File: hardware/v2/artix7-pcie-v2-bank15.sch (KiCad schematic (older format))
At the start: 1 part, among them U1 XC7A75T-FGG484

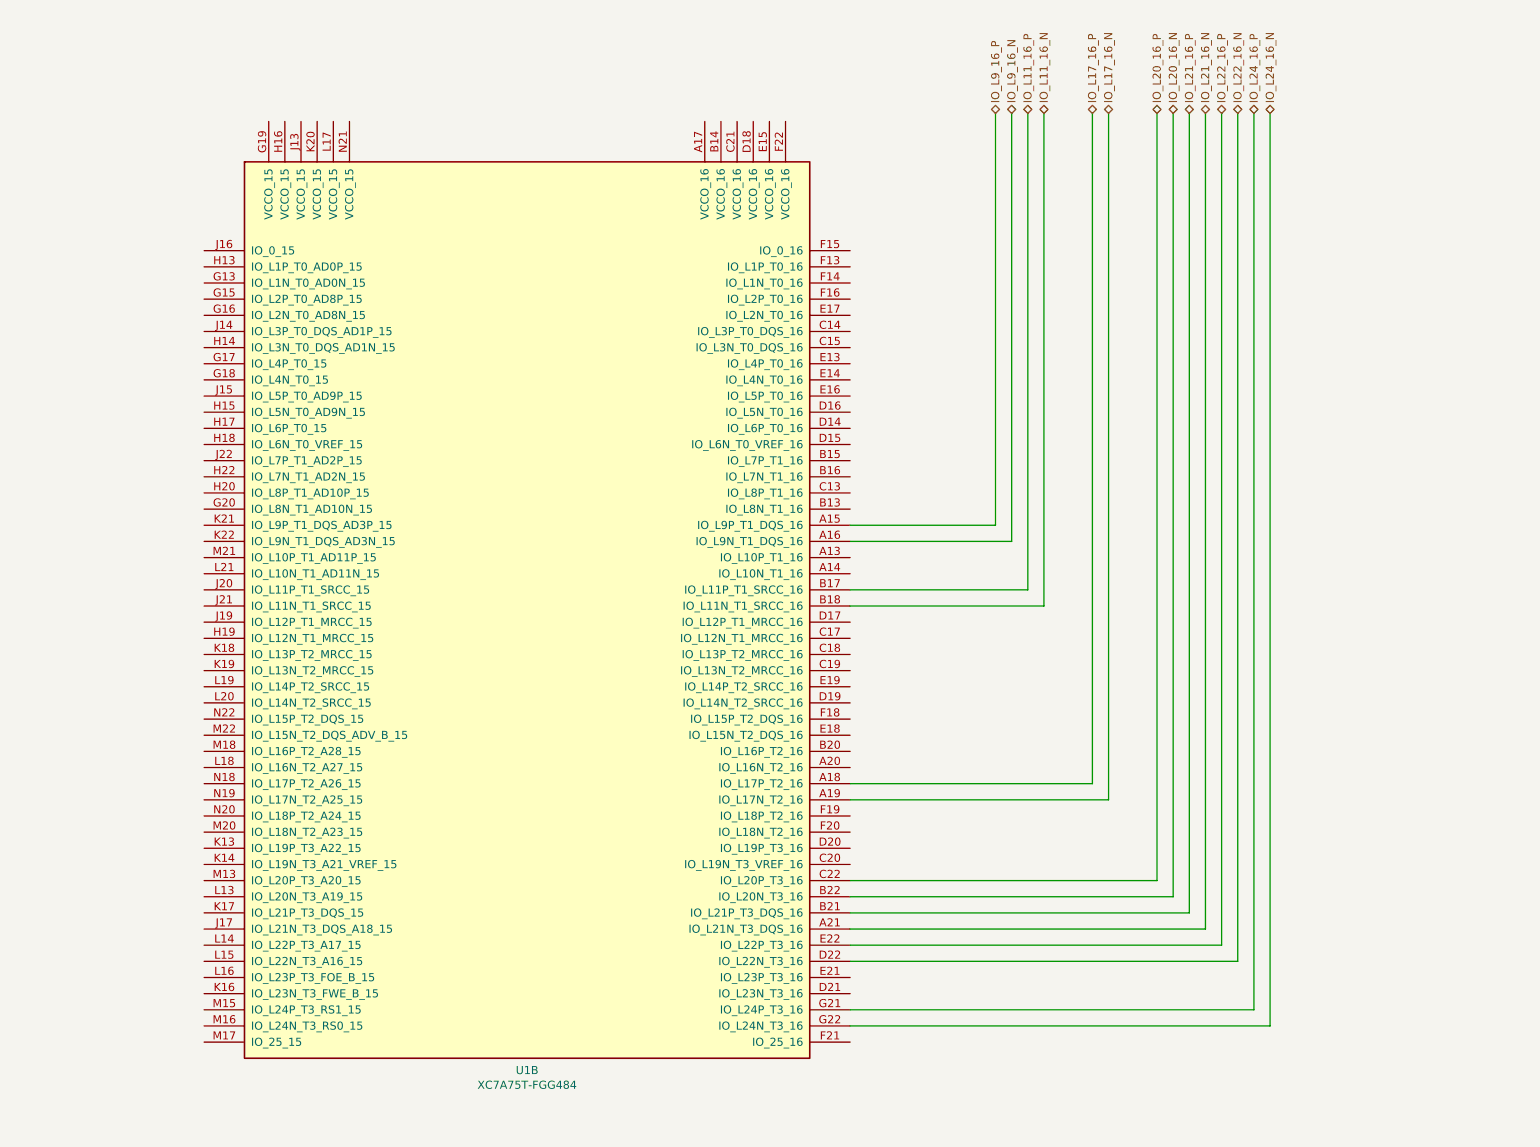
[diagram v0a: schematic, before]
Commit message: v2 schematic/pcb: band 13 to NC for smaller device compatibility
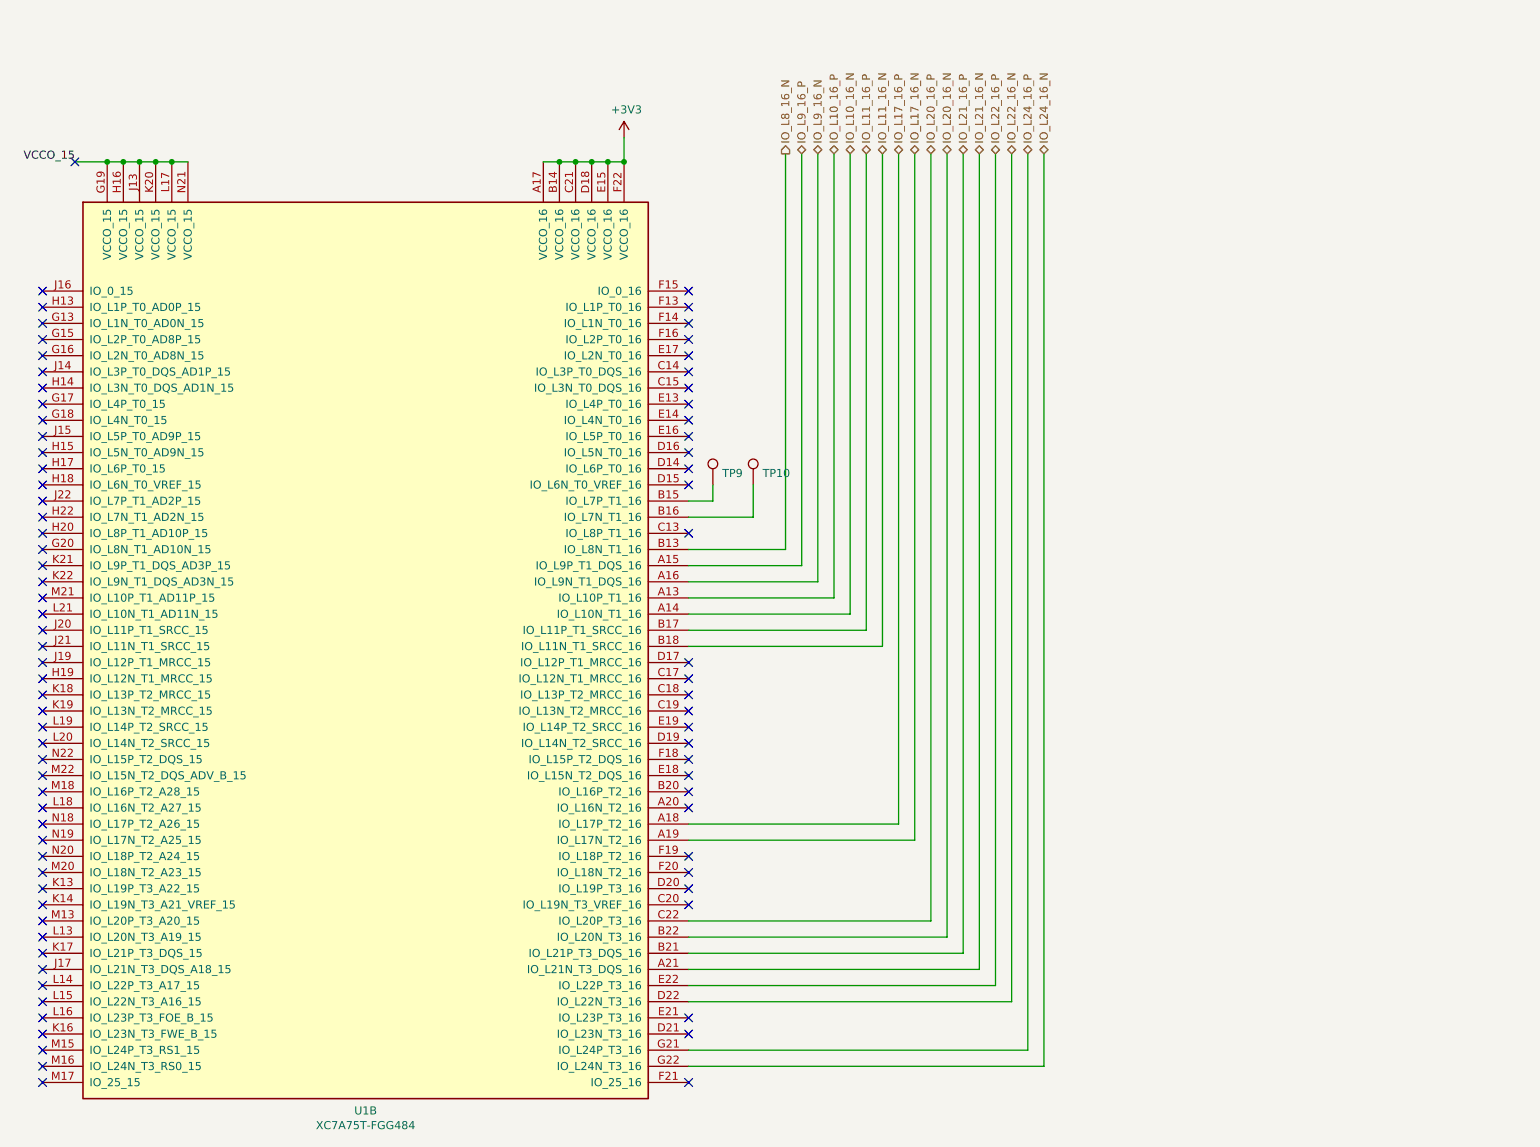
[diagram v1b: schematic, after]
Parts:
- added TP10, TP9: TestPoint, tom-mechanical:TestPoint_Pad_D1.5mm, symbol tom-mechanical:TestPoint
- U1: footprint (none) -> artix7-pcie-v2:Xilinx_FGG484
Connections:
- net IO_L10_16_P: now reaches U1.A13 (IO_L10P_T1_16)
- net IO_L10_16_N: now reaches U1.A14 (IO_L10N_T1_16)
- net +3V3: now reaches U1.A17 (VCCO_16)
- net +3V3: now also U1.B14 (VCCO_16), U1.C21 (VCCO_16), U1.D18 (VCCO_16), U1.E15 (VCCO_16), U1.F22 (VCCO_16)
- net IO_L8_16_N: now reaches U1.B13 (IO_L8N_T1_16)
- net at U1.B15 (IO_L7P_T1_16): now also TP9.1
- net at U1.B16 (IO_L7N_T1_16): now also TP10.1
- net VCCO_15: now reaches U1.G19 (VCCO_15)
- net VCCO_15: now also U1.H16 (VCCO_15), U1.J13 (VCCO_15), U1.K20 (VCCO_15), U1.L17 (VCCO_15), U1.N21 (VCCO_15)
- no-connect marks 0 -> 82
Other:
- moved on the sheet: U1B

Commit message: v2 hardware progress checkin, just prior to replacing p/s with TI parts
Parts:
- renumbered TP9 to TP5, TP10 to TP6
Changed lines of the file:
@@
 	5150 3900 4550 3900
 $Comp
-L tom-mechanical:TestPoint TP9
+L tom-mechanical:TestPoint TP5
 U 1 1 5F434414
 P 4700 3500
-F 0 "TP9" H 4758 3572 50  0000 L CNN
+F 0 "TP5" H 4758 3572 50  0000 L CNN
 F 1 "TestPoint" H 4758 3527 50  0001 L CNN
 F 2 "tom-mechanical:TestPoint_Pad_D1.5mm" H 4758 3527 50  0001 L CNN
@@
 $EndComp
 $Comp
-L tom-mechanical:TestPoint TP10
+L tom-mechanical:TestPoint TP6
 U 1 1 5F435AEE
 P 4950 3500
-F 0 "TP10" H 5008 3572 50  0000 L CNN
+F 0 "TP6" H 5008 3572 50  0000 L CNN
 F 1 "TestPoint" H 5008 3527 50  0001 L CNN
 F 2 "tom-mechanical:TestPoint_Pad_D1.5mm" H 5008 3527 50  0001 L CNN

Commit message: v2 pcb/schematic update : drc passing, need to add caps
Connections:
- net +3V3 renamed VCCO_16
- net IO_L10_16_N: no longer names the net of U1.A14 (IO_L10N_T1_16)
- net IO_L10_16_P: no longer names the net of U1.A13 (IO_L10P_T1_16)
- net IO_L8_16_N: no longer names the net of U1.B13 (IO_L8N_T1_16)
- no-connect marks 82 -> 84
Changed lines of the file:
@@
 EESchema Schematic File Version 4
-LIBS:artix7-pcie-v2-cache
 EELAYER 30 0
 EELAYER END
 $Descr A4 11693 8268
 encoding utf-8
-Sheet 5 7
+Sheet 3 7
 Title ""
 Date ""
@@
 Wire Wire Line
 	4050 1500 4150 1500
-$Comp
-L power:+3V3 #PWR0122
-U 1 1 5F15DFBC
-P 4150 1350
-F 0 "#PWR0122" H 4150 1200 50  0001 C CNN
-F 1 "+3V3" H 4165 1523 50  0000 C CNN
-F 2 "" H 4150 1350 50  0001 C CNN
-F 3 "" H 4150 1350 50  0001 C CNN
-	1    4150 1350
-	1    0    0    -1
-$EndComp
 Wire Wire Line
 	4550 5700 5950 5700
@@
 Wire Wire Line
 	1450 1500 1350 1500
-Connection ~ 950  1500
-Wire Wire Line
-	950  1500 750  1500
 Connection ~ 1050 1500
 Wire Wire Line
@@
 Wire Wire Line
 	1350 1500 1250 1500
-NoConn ~ 750  1500
-Text Label 750  1500 2    50   ~ 0
+Text Label 1450 1500 0    50   ~ 0
 VCCO_15
-Text HLabel 5450 1450 1    50   BiDi ~ 0
-IO_L10_16_P
-Text HLabel 5550 1450 1    50   BiDi ~ 0
-IO_L10_16_N
-Wire Wire Line
-	4550 4200 5450 4200
-Wire Wire Line
-	5450 4200 5450 1450
-Wire Wire Line
-	5550 1450 5550 4300
-Wire Wire Line
-	5550 4300 4550 4300
-Text HLabel 5150 1450 1    50   Output ~ 0
-IO_L8_16_N
-Wire Wire Line
-	5150 1450 5150 3900
-Wire Wire Line
-	5150 3900 4550 3900
 $Comp
 L tom-mechanical:TestPoint TP5
@@
 Wire Wire Line
 	4950 3700 4950 3500
+Text HLabel 4150 1350 1    50   Input ~ 0
+VCCO_16
+NoConn ~ 4550 4200
+NoConn ~ 4550 4300
+NoConn ~ 4550 3900
+$Comp
+L power:PWR_FLAG #FLG0111
+U 1 1 5EE4B316
+P 950 1500
+F 0 "#FLG0111" H 950 1575 50  0001 C CNN
+F 1 "PWR_FLAG" H 950 1673 50  0000 C CNN
+F 2 "" H 950 1500 50  0001 C CNN
+F 3 "~" H 950 1500 50  0001 C CNN
+	1    950  1500
+	1    0    0    -1
+$EndComp
+Connection ~ 950  1500
 $EndSCHEMATC

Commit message: v2 hardware: pcb progress commit, 155 unrouted
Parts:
- added C78: 100uF/6.3V/X5R, tom-passives:C_1206_3216Metric, symbol tom-passives:C
- added C79, C80: 4.7uF/6.3V/X5R, tom-passives:C_0402_1005Metric, symbol tom-passives:C
- added C81, C82, C83, C84: 0.47uF/6.3V/X5R, tom-passives:C_0402_1005Metric, symbol tom-passives:C
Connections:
- net VCCO_16: now also C78.1, C79.1, C80.1, C81.1, C82.1, C83.1, C84.1
- new net GND: C78.2, C79.2, C80.2, C81.2, C82.2, C83.2, C84.2
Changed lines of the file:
@@
 $EndComp
 Connection ~ 950  1500
+$Comp
+L tom-passives:C C?
+U 1 1 5E9DF380
+P 8450 2000
+AR Path="/5E98B37D/5E9DF380" Ref="C?"  Part="1"
+AR Path="/5E48AFE6/5F1FEEB3/5E9DF380" Ref="C?"  Part="1"
+AR Path="/5E5E2B54/5E9DF380" Ref="C?"  Part="1"
+AR Path="/5ED151B3/5E9DF380" Ref="C78"  Part="1"
+F 0 "C78" V 8400 1200 40  0000 L CNN
+F 1 "100uF/6.3V/X5R" V 8500 1200 40  0000 L CNN
+F 2 "tom-passives:C_1206_3216Metric" H 8488 1850 30  0001 C CNN
+F 3 "" H 8450 2000 60  0001 C CNN
+	1    8450 2000
+	1    0    0    -1
+$EndComp
+$Comp
+L tom-passives:C C?
+U 1 1 5E9DF386
+P 8650 2000
+AR Path="/5E98B37D/5E9DF386" Ref="C?"  Part="1"
+AR Path="/5E48AFE6/5F1FEEB3/5E9DF386" Ref="C?"  Part="1"
+AR Path="/5E5E2B54/5E9DF386" Ref="C?"  Part="1"
+AR Path="/5ED151B3/5E9DF386" Ref="C79"  Part="1"
+F 0 "C79" V 8600 1200 40  0000 L CNN
+F 1 "4.7uF/6.3V/X5R" V 8700 1200 40  0000 L CNN
+F 2 "tom-passives:C_0402_1005Metric" H 8688 1850 30  0001 C CNN
+F 3 "" H 8650 2000 60  0001 C CNN
+	1    8650 2000
+	1    0    0    -1
+$EndComp
+Wire Wire Line
+	8200 1800 8450 1800
+Connection ~ 8450 1800
+Wire Wire Line
+	8450 1800 8650 1800
+Wire Wire Line
+	8200 2200 8450 2200
+Connection ~ 8450 2200
+Wire Wire Line
+	8450 2200 8650 2200
+$Comp
+L tom-passives:C C?
+U 1 1 5E9DF392
+P 8850 2000
+AR Path="/5E98B37D/5E9DF392" Ref="C?"  Part="1"
+AR Path="/5E48AFE6/5F1FEEB3/5E9DF392" Ref="C?"  Part="1"
+AR Path="/5E5E2B54/5E9DF392" Ref="C?"  Part="1"
+AR Path="/5ED151B3/5E9DF392" Ref="C80"  Part="1"
+F 0 "C80" V 8800 1200 40  0000 L CNN
+F 1 "4.7uF/6.3V/X5R" V 8900 1200 40  0000 L CNN
+F 2 "tom-passives:C_0402_1005Metric" H 8888 1850 30  0001 C CNN
+F 3 "" H 8850 2000 60  0001 C CNN
+	1    8850 2000
+	1    0    0    -1
+$EndComp
+Wire Wire Line
+	8650 1800 8850 1800
+Connection ~ 8650 1800
+Wire Wire Line
+	8650 2200 8850 2200
+Connection ~ 8650 2200
+$Comp
+L tom-passives:C C?
+U 1 1 5E9DF39C
+P 9050 2000
+AR Path="/5E98B37D/5E9DF39C" Ref="C?"  Part="1"
+AR Path="/5E48AFE6/5F1FEEB3/5E9DF39C" Ref="C?"  Part="1"
+AR Path="/5E5E2B54/5E9DF39C" Ref="C?"  Part="1"
+AR Path="/5ED151B3/5E9DF39C" Ref="C81"  Part="1"
+F 0 "C81" V 9000 1200 40  0000 L CNN
+F 1 "0.47uF/6.3V/X5R" V 9100 1200 40  0000 L CNN
+F 2 "tom-passives:C_0402_1005Metric" H 9088 1850 30  0001 C CNN
+F 3 "" H 9050 2000 60  0001 C CNN
+	1    9050 2000
+	1    0    0    -1
+$EndComp
+$Comp
+L tom-passives:C C?
+U 1 1 5E9DF3A2
+P 9250 2000
+AR Path="/5E98B37D/5E9DF3A2" Ref="C?"  Part="1"
+AR Path="/5E48AFE6/5F1FEEB3/5E9DF3A2" Ref="C?"  Part="1"
+AR Path="/5E5E2B54/5E9DF3A2" Ref="C?"  Part="1"
+AR Path="/5ED151B3/5E9DF3A2" Ref="C82"  Part="1"
+F 0 "C82" V 9200 1200 40  0000 L CNN
+F 1 "0.47uF/6.3V/X5R" V 9300 1200 40  0000 L CNN
+F 2 "tom-passives:C_0402_1005Metric" H 9288 1850 30  0001 C CNN
+F 3 "" H 9250 2000 60  0001 C CNN
+	1    9250 2000
+	1    0    0    -1
+$EndComp
+$Comp
+L tom-passives:C C?
+U 1 1 5E9DF3A8
+P 9450 2000
+AR Path="/5E98B37D/5E9DF3A8" Ref="C?"  Part="1"
+AR Path="/5E48AFE6/5F1FEEB3/5E9DF3A8" Ref="C?"  Part="1"
+AR Path="/5E5E2B54/5E9DF3A8" Ref="C?"  Part="1"
+AR Path="/5ED151B3/5E9DF3A8" Ref="C83"  Part="1"
+F 0 "C83" V 9400 1200 40  0000 L CNN
+F 1 "0.47uF/6.3V/X5R" V 9500 1200 40  0000 L CNN
+F 2 "tom-passives:C_0402_1005Metric" H 9488 1850 30  0001 C CNN
+F 3 "" H 9450 2000 60  0001 C CNN
+	1    9450 2000
+	1    0    0    -1
+$EndComp
+$Comp
+L tom-passives:C C?
+U 1 1 5E9DF3AE
+P 9650 2000
+AR Path="/5E98B37D/5E9DF3AE" Ref="C?"  Part="1"
+AR Path="/5E48AFE6/5F1FEEB3/5E9DF3AE" Ref="C?"  Part="1"
+AR Path="/5E5E2B54/5E9DF3AE" Ref="C?"  Part="1"
+AR Path="/5ED151B3/5E9DF3AE" Ref="C84"  Part="1"
+F 0 "C84" V 9600 1200 40  0000 L CNN
+F 1 "0.47uF/6.3V/X5R" V 9700 1200 40  0000 L CNN
+F 2 "tom-passives:C_0402_1005Metric" H 9688 1850 30  0001 C CNN
+F 3 "" H 9650 2000 60  0001 C CNN
+	1    9650 2000
+	1    0    0    -1
+$EndComp
+Connection ~ 9050 1800
+Wire Wire Line
+	9050 1800 9250 1800
+Connection ~ 9250 1800
+Wire Wire Line
+	9250 1800 9450 1800
+Connection ~ 9450 1800
+Wire Wire Line
+	9450 1800 9650 1800
+Connection ~ 9050 2200
+Wire Wire Line
+	9050 2200 9250 2200
+Connection ~ 9250 2200
+Wire Wire Line
+	9250 2200 9450 2200
+Connection ~ 9450 2200
+Wire Wire Line
+	9450 2200 9650 2200
+Connection ~ 8850 1800
+Connection ~ 8850 2200
+Wire Wire Line
+	8850 1800 9050 1800
+Wire Wire Line
+	8850 2200 9050 2200
+$Comp
+L power:GND #PWR?
+U 1 1 5E9DF3C4
+P 8200 2200
+AR Path="/5E5E2B54/5E9DF3C4" Ref="#PWR?"  Part="1"
+AR Path="/5ED151B3/5E9DF3C4" Ref="#PWR039"  Part="1"
+F 0 "#PWR039" H 8200 1950 50  0001 C CNN
+F 1 "GND" H 8205 2027 50  0000 C CNN
+F 2 "" H 8200 2200 50  0001 C CNN
+F 3 "" H 8200 2200 50  0001 C CNN
+	1    8200 2200
+	1    0    0    -1
+$EndComp
+Text Label 8200 1800 2    50   ~ 0
+VCCO_16
+Text Label 3650 1500 2    50   ~ 0
+VCCO_16
 $EndSCHEMATC

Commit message: v2 pcb/schematic progress commit, all tough signals routed out
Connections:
- net IO_L23_16_N: now reaches U1.D21 (IO_L23N_T3_16)
- net IO_L23_16_P: now reaches U1.E21 (IO_L23P_T3_16)
- net IO_L9_16_N: no longer names the net of U1.A16 (IO_L9N_T1_DQS_16)
- net IO_L9_16_P: no longer names the net of U1.A15 (IO_L9P_T1_DQS_16)
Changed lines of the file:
@@
 	1    0    0    -1
 $EndComp
-Text HLabel 5250 1450 1    50   BiDi ~ 0
-IO_L9_16_P
-Wire Wire Line
-	5250 1450 5250 4000
-Wire Wire Line
-	5250 4000 4550 4000
-Text HLabel 5350 1450 1    50   BiDi ~ 0
-IO_L9_16_N
-Wire Wire Line
-	5350 1450 5350 4100
-Wire Wire Line
-	5350 4100 4550 4100
-Text HLabel 5650 1450 1    50   BiDi ~ 0
-IO_L11_16_P
-Text HLabel 5750 1450 1    50   BiDi ~ 0
-IO_L11_16_N
 Text HLabel 6050 1450 1    50   BiDi ~ 0
 IO_L20_16_P
@@
 	5650 1450 5650 4400
 Wire Wire Line
-	5650 4400 4550 4400
-Wire Wire Line
-	4550 4500 5750 4500
-Wire Wire Line
 	5750 4500 5750 1450
-Text HLabel 6650 1450 1    50   BiDi ~ 0
-IO_L24_16_P
-Text HLabel 6750 1450 1    50   BiDi ~ 0
-IO_L24_16_N
 Wire Wire Line
 	6050 6200 4550 6200
@@
 	4550 6500 6350 6500
 Wire Wire Line
-	6650 1450 6650 7000
-Wire Wire Line
-	6650 7000 4550 7000
-Wire Wire Line
-	4550 7100 6750 7100
-Wire Wire Line
-	6750 7100 6750 1450
+	6850 7000 4550 7000
+Wire Wire Line
+	4550 7100 6950 7100
 Text HLabel 6550 1450 1    50   BiDi ~ 0
 IO_L22_16_N
@@
 NoConn ~ 4550 6000
 NoConn ~ 4550 6100
-NoConn ~ 4550 6800
-NoConn ~ 4550 6900
 NoConn ~ 4550 7200
 NoConn ~ 550  2300
@@
 Text Label 3650 1500 2    50   ~ 0
 VCCO_16
+Wire Wire Line
+	6950 7100 6950 1450
+Wire Wire Line
+	6850 1450 6850 7000
+Text HLabel 6950 1450 1    50   BiDi ~ 0
+IO_L24_16_N
+Text HLabel 6850 1450 1    50   BiDi ~ 0
+IO_L24_16_P
+Text HLabel 6750 1450 1    50   BiDi ~ 0
+IO_L23_16_N
+Text HLabel 6650 1450 1    50   BiDi ~ 0
+IO_L23_16_P
+Wire Wire Line
+	4550 6800 6650 6800
+Wire Wire Line
+	4550 6900 6750 6900
+Wire Wire Line
+	6650 6800 6650 1450
+Wire Wire Line
+	6750 1450 6750 6900
+NoConn ~ 4550 4000
+NoConn ~ 4550 4100
+Wire Wire Line
+	4550 4500 5750 4500
+Wire Wire Line
+	5650 4400 4550 4400
+Text HLabel 5750 1450 1    50   BiDi ~ 0
+IO_L11_16_N
+Text HLabel 5650 1450 1    50   BiDi ~ 0
+IO_L11_16_P
 $EndSCHEMATC

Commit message: v2 schematic/pcb progress commit - 12 unrouted
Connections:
- net IO_L9_16_N: now reaches U1.A15 (IO_L9P_T1_DQS_16)
- net IO_L9_16_P: now reaches U1.A16 (IO_L9N_T1_DQS_16)
- net IO_L23_16_N: no longer names the net of U1.D21 (IO_L23N_T3_16)
- net IO_L23_16_P: no longer names the net of U1.E21 (IO_L23P_T3_16)
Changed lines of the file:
@@
 Text HLabel 6850 1450 1    50   BiDi ~ 0
 IO_L24_16_P
-Text HLabel 6750 1450 1    50   BiDi ~ 0
-IO_L23_16_N
-Text HLabel 6650 1450 1    50   BiDi ~ 0
-IO_L23_16_P
-Wire Wire Line
-	4550 6800 6650 6800
-Wire Wire Line
-	4550 6900 6750 6900
-Wire Wire Line
-	6650 6800 6650 1450
-Wire Wire Line
-	6750 1450 6750 6900
-NoConn ~ 4550 4000
-NoConn ~ 4550 4100
+Text HLabel 5450 1450 1    50   BiDi ~ 0
+IO_L9_16_N
+Text HLabel 5550 1450 1    50   BiDi ~ 0
+IO_L9_16_P
 Wire Wire Line
 	4550 4500 5750 4500
@@
 Text HLabel 5650 1450 1    50   BiDi ~ 0
 IO_L11_16_P
+Wire Wire Line
+	5550 1450 5550 4100
+Wire Wire Line
+	5550 4100 4550 4100
+Wire Wire Line
+	4550 4000 5450 4000
+Wire Wire Line
+	5450 4000 5450 1450
+NoConn ~ 4550 6800
+NoConn ~ 4550 6900
 $EndSCHEMATC

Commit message: v2 hardware: add Digikey part numbers to schematic and generate bom
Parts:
- C78: Vendor (none) -> 478-12404-1-ND
- C79, C80: Vendor (none) -> 490-5915-1-ND
- C81, C82, C83, C84: Vendor (none) -> 1276-CL05Y474KP5VPNCCT-ND
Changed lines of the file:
@@
 F 2 "tom-passives:C_1206_3216Metric" H 8488 1850 30  0001 C CNN
 F 3 "" H 8450 2000 60  0001 C CNN
+F 4 "478-12404-1-ND" H 8450 2000 50  0001 C CNN "Vendor"
 	1    8450 2000
 	1    0    0    -1
@@
 F 2 "tom-passives:C_0402_1005Metric" H 8688 1850 30  0001 C CNN
 F 3 "" H 8650 2000 60  0001 C CNN
+F 4 "490-5915-1-ND" H 8650 2000 50  0001 C CNN "Vendor"
 	1    8650 2000
 	1    0    0    -1
@@
 F 2 "tom-passives:C_0402_1005Metric" H 8888 1850 30  0001 C CNN
 F 3 "" H 8850 2000 60  0001 C CNN
+F 4 "490-5915-1-ND" H 8850 2000 50  0001 C CNN "Vendor"
 	1    8850 2000
 	1    0    0    -1
@@
 F 2 "tom-passives:C_0402_1005Metric" H 9088 1850 30  0001 C CNN
 F 3 "" H 9050 2000 60  0001 C CNN
+F 4 "1276-CL05Y474KP5VPNCCT-ND" H 9050 2000 50  0001 C CNN "Vendor"
 	1    9050 2000
 	1    0    0    -1
@@
 F 2 "tom-passives:C_0402_1005Metric" H 9288 1850 30  0001 C CNN
 F 3 "" H 9250 2000 60  0001 C CNN
+F 4 "1276-CL05Y474KP5VPNCCT-ND" H 9250 2000 50  0001 C CNN "Vendor"
 	1    9250 2000
 	1    0    0    -1
@@
 F 2 "tom-passives:C_0402_1005Metric" H 9488 1850 30  0001 C CNN
 F 3 "" H 9450 2000 60  0001 C CNN
+F 4 "1276-CL05Y474KP5VPNCCT-ND" H 9450 2000 50  0001 C CNN "Vendor"
 	1    9450 2000
 	1    0    0    -1
@@
 F 2 "tom-passives:C_0402_1005Metric" H 9688 1850 30  0001 C CNN
 F 3 "" H 9650 2000 60  0001 C CNN
+F 4 "1276-CL05Y474KP5VPNCCT-ND" H 9650 2000 50  0001 C CNN "Vendor"
 	1    9650 2000
 	1    0    0    -1

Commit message: v2 hardware: aug2020 pcb updates
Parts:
- C78: footprint tom-passives:C_1206_3216Metric -> tom-passives:CP_EIA-3216-12_Kemet-S; symbol tom-passives:C -> tom-passives:CP_Small
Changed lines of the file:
@@
 Connection ~ 950  1500
 $Comp
-L tom-passives:C C?
+L tom-passives:CP_Small C?
 U 1 1 5E9DF380
 P 8450 2000
@@
 F 0 "C78" V 8400 1200 40  0000 L CNN
 F 1 "100uF/6.3V/X5R" V 8500 1200 40  0000 L CNN
-F 2 "tom-passives:C_1206_3216Metric" H 8488 1850 30  0001 C CNN
+F 2 "tom-passives:CP_EIA-3216-12_Kemet-S" H 8488 1850 30  0001 C CNN
 F 3 "" H 8450 2000 60  0001 C CNN
 F 4 "478-12404-1-ND" H 8450 2000 50  0001 C CNN "Vendor"
@@
 Wire Wire Line
 	8450 1800 8650 1800
-Wire Wire Line
-	8200 2200 8450 2200
-Connection ~ 8450 2200
-Wire Wire Line
-	8450 2200 8650 2200
 $Comp
 L tom-passives:C C?
@@
 NoConn ~ 4550 6800
 NoConn ~ 4550 6900
+Wire Wire Line
+	8450 1800 8450 1900
+Wire Wire Line
+	8200 2200 8450 2200
+Wire Wire Line
+	8450 2100 8450 2200
+Connection ~ 8450 2200
+Wire Wire Line
+	8450 2200 8650 2200
 $EndSCHEMATC
